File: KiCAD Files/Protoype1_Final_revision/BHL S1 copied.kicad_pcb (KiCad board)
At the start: 4 copper layers, 64 x 64 mm, 104 parts, among them IC1 NUP2105LT1G, IC2 NUP2105LT1G, IC4 FD6288Q, J1 39-30-1042, J2 Conn_01x03_Pin, J3 Conn_01x03_Pin, J4 39-30-1042, Q1 CSD19502Q5B, Q2 CSD19502Q5B, Q3 CSD19502Q5B, Q4 CSD19502Q5B, Q5 CSD19502Q5B, Q7 CSD19502Q5B, SW1 PTS636 SM50J SMTR LFS, U1 ME6211C30M5, U2 SPX3819M5-L-5-0, U3 Solder Pad, U5 STM32G431CBU6, Y1 8MHz

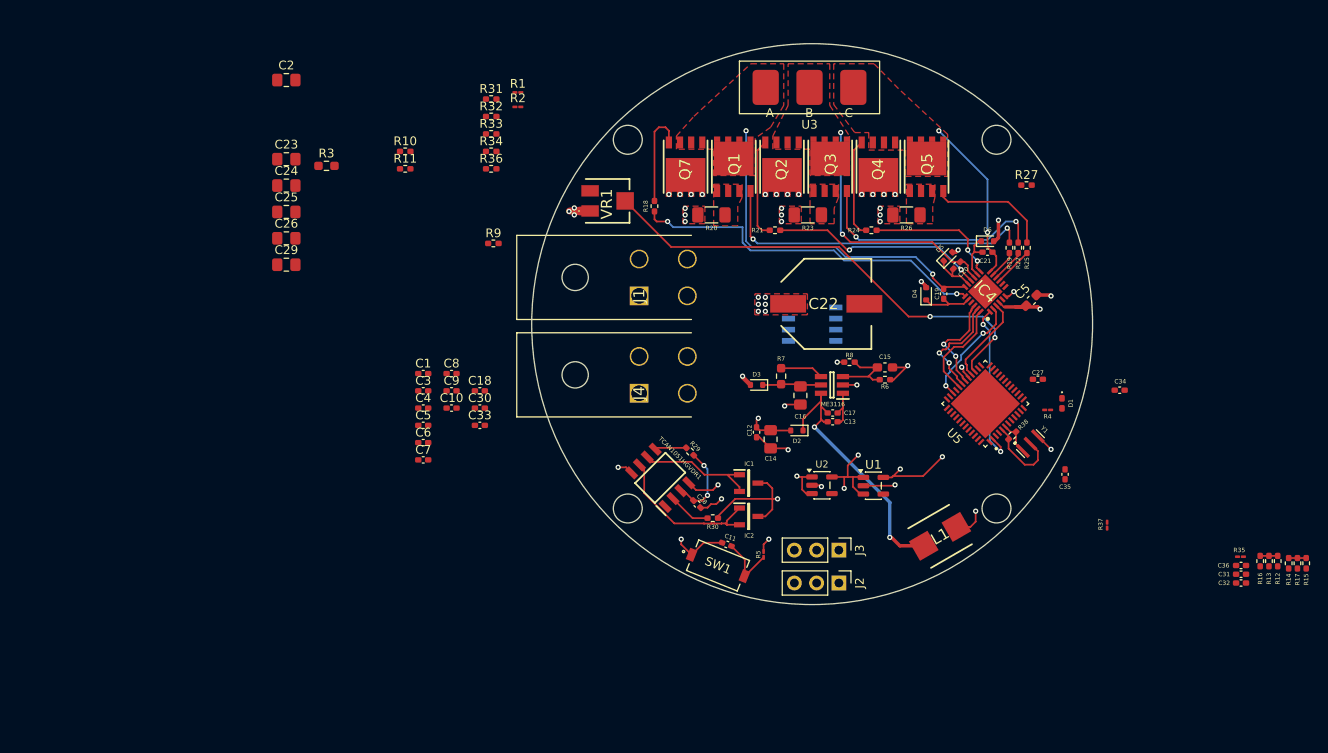
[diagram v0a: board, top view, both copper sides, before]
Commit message: Finished Routing the Magnetic Encoder and part of the STM32
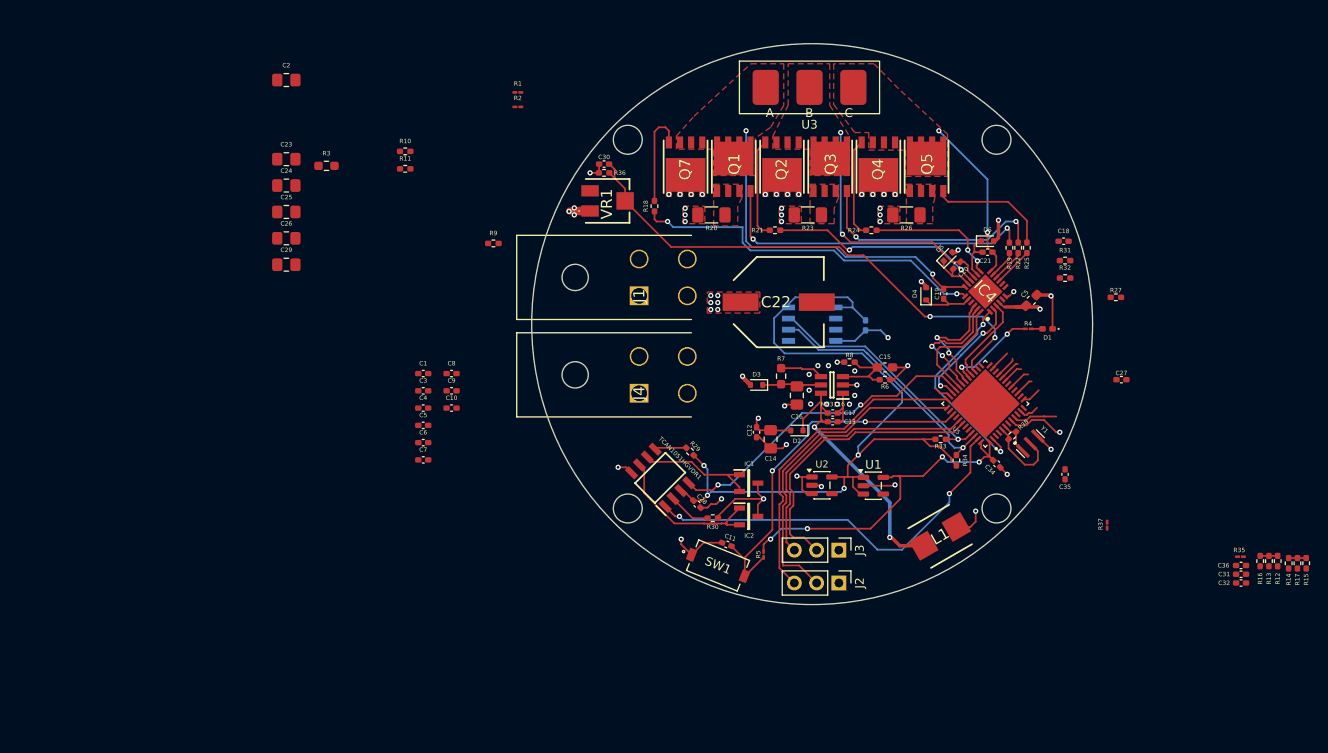
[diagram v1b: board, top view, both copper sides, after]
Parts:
- C33: moved to B.Cu
- moved C18 68.8 mm to (226.4, 74.0)
- moved R31 68.0 mm to (226.6, 76.2)
- moved R32 68.0 mm to (226.6, 78.2)
- moved R34 63.7 mm to (214.2, 99.0), turned to -90 degrees
- moved R33 62.0 mm to (212.4, 96.6), turned to 180 degrees
- moved C33 45.5 mm to (203.8, 83.6), turned to -90 degrees
- moved C30 31.2 mm to (174.0, 65.2), turned to 180 degrees
- moved R27 16.4 mm to (232.4, 80.4)
- moved C34 16.4 mm to (218.8, 99.4), turned to -45 degrees
- moved R36 12.9 mm to (174.0, 66.2)
- moved C27 9.53 mm to (233.0, 89.8)
- moved R4 9.51 mm to (222.4, 84.0)
- moved D1 8.66 mm to (224.6, 84.0), turned to 180 degrees
- moved C22 5.43 mm to (193.9, 81.0)
- moved C16 0.40 mm to (196.0, 91.6)
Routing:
- net VCC_5V: track 35.5 -> 94.1 mm
- net CAN_TX: track 0.00 -> 45.3 mm, vias 0 -> 2
- net SWCLK: track 0.00 -> 37.5 mm
- net SWDIO: track 0.00 -> 36.5 mm
- net BUTTON: track 7.15 -> 42.5 mm, vias 0 -> 2
- net Net-(J3-Pin_2): track 0.00 -> 33.2 mm
- net CAN_RX: track 3.93 -> 36.9 mm, vias 1 -> 2
- net USART2_TX: track 0.00 -> 31.8 mm
- net SDA: track 0.00 -> 29.1 mm, vias 0 -> 1
- net SCLK: track 0.00 -> 28.3 mm, vias 0 -> 1
- net GND: track 48.8 -> 65.9 mm, vias 22 -> 35
- net +3.3V: track 30.0 -> 43.6 mm, vias 3 -> 4
- net STATUS: track 1.59 -> 10.6 mm, vias 1 -> 2
- net VBUS: track 0.00 -> 6.60 mm, vias 0 -> 1
- net TEMP_FEEDBACK: track 54.4 -> 60.2 mm
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
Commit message: Finished the Board!!
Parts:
- removed C10, C6, C7, C8, C9: 0.1uF, Capacitor_SMD:C_0402_1005Metric_Pad0.74x0.62mm_HandSolder
- removed C29: 10uF/35V, Capacitor_SMD:C_0805_2012Metric_Pad1.18x1.45mm_HandSolder
- removed the C5 at (153.4, 95.0)
- removed R1: 0, Resistor_SMD:R_01005_0402Metric_Pad0.57x0.30mm_HandSolder
- removed R2: 10K, Resistor_SMD:R_01005_0402Metric_Pad0.57x0.30mm_HandSolder
- removed R27: 0, Resistor_SMD:R_0402_1005Metric_Pad0.72x0.64mm_HandSolder
- removed R3: 1M, Resistor_SMD:R_0603_1608Metric_Pad0.98x0.95mm_HandSolder
- C2: footprint Capacitor_SMD:C_0805_2012Metric_Pad1.18x1.45mm_HandSolder -> Capacitor_SMD:C_0402_1005Metric_Pad0.74x0.62mm_HandSolder
- moved C2 85.9 mm to (208.6, 104.2), turned to -90 degrees
- moved R10 80.8 mm to (226.6, 93.0), turned to 45 degrees
- moved R11 79.2 mm to (225.9, 92.3), turned to -135 degrees
- moved R9 67.7 mm to (228.6, 82.2), turned to 90 degrees
- moved C1 58.2 mm to (209.6, 104.2), turned to -90 degrees
- moved C23 56.4 mm to (188.2, 89.8)
- moved C24 55.9 mm to (188.2, 91.8)
- moved C25 55.5 mm to (188.2, 93.8)
- moved C26 55.1 mm to (188.2, 95.8)
- moved C3 51.1 mm to (202.8, 104.2), turned to -90 degrees
- moved C4 49.7 mm to (201.8, 104.2), turned to -90 degrees
- moved R15 39.7 mm to (226.6, 82.2), turned to 90 degrees
- moved R12 36.6 mm to (227.6, 82.2), turned to 90 degrees
- moved C36 36.0 mm to (220.6, 86.2), turned to 45 degrees
- moved R17 35.8 mm to (227.0, 86.2), turned to -90 degrees
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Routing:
- net +3.3V: track 43.6 -> 110.0 mm, vias 4 -> 7
- net Vshunt_1+: track 0.00 -> 51.8 mm, vias 0 -> 2
- net GND: track 65.9 -> 114.8 mm, vias 35 -> 54
- net Vshunt_2+: track 0.00 -> 39.5 mm, vias 0 -> 2
- net CAN_H: track 18.4 -> 57.4 mm
- net VBUS: track 6.60 -> 44.0 mm, vias 1 -> 2
- net VCC_12V: track 65.0 -> 100.5 mm
- net Vshunt_3+: track 0.00 -> 27.9 mm, vias 0 -> 2
- net CAN_L: track 14.0 -> 41.4 mm
- net DCBUS: track 5.17 -> 21.7 mm, vias 22 -> 26
- net Curr_fdbk1_OPAmp+: track 5.11 -> 21.0 mm, vias 0 -> 2
- net Net-(U5-PG10-~{RST}): track 0.00 -> 14.3 mm
- net Curr_fdbk3_OPAmp+: track 4.53 -> 18.5 mm, vias 0 -> 2
- net Curr_fdbk2_OPAmp+: track 4.19 -> 17.5 mm, vias 0 -> 2
- net Net-(U5-VDDA): track 4.92 -> 12.1 mm
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
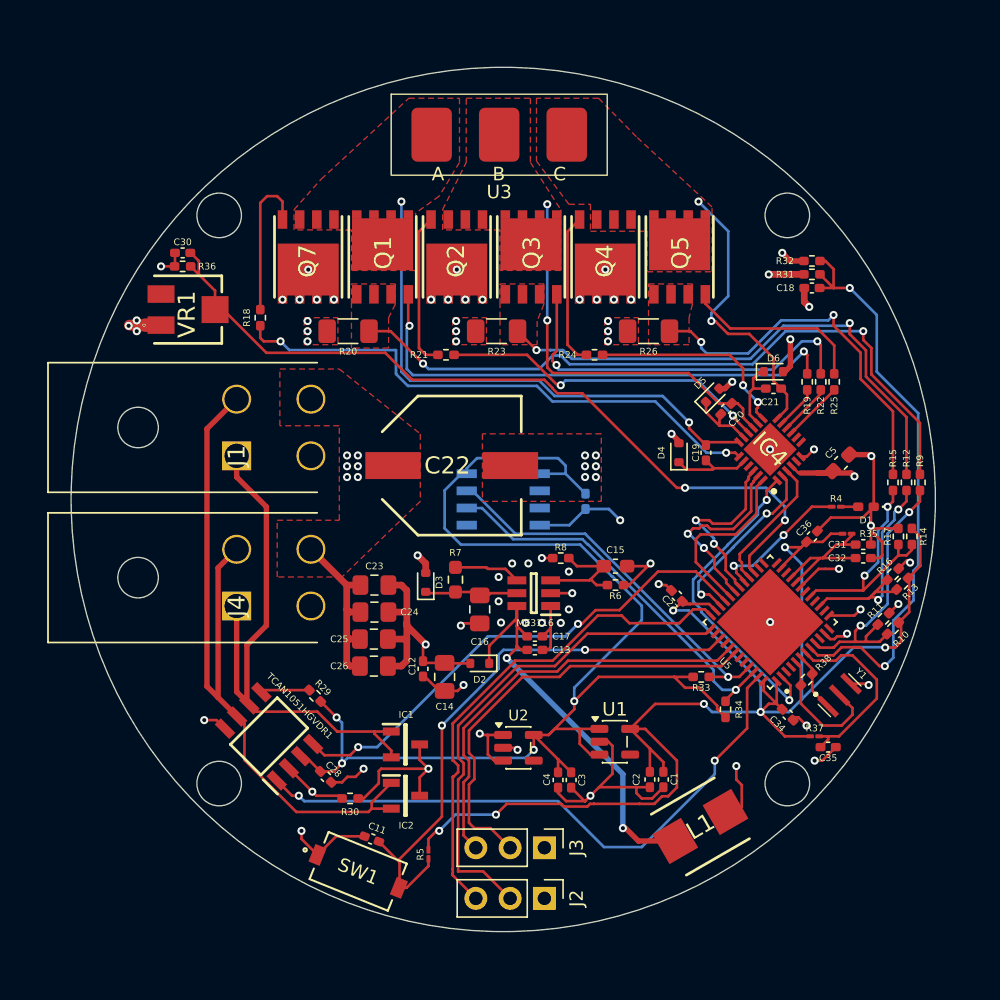
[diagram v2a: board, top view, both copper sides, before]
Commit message: Finished PCB. Enlargened diameter to 70mm.
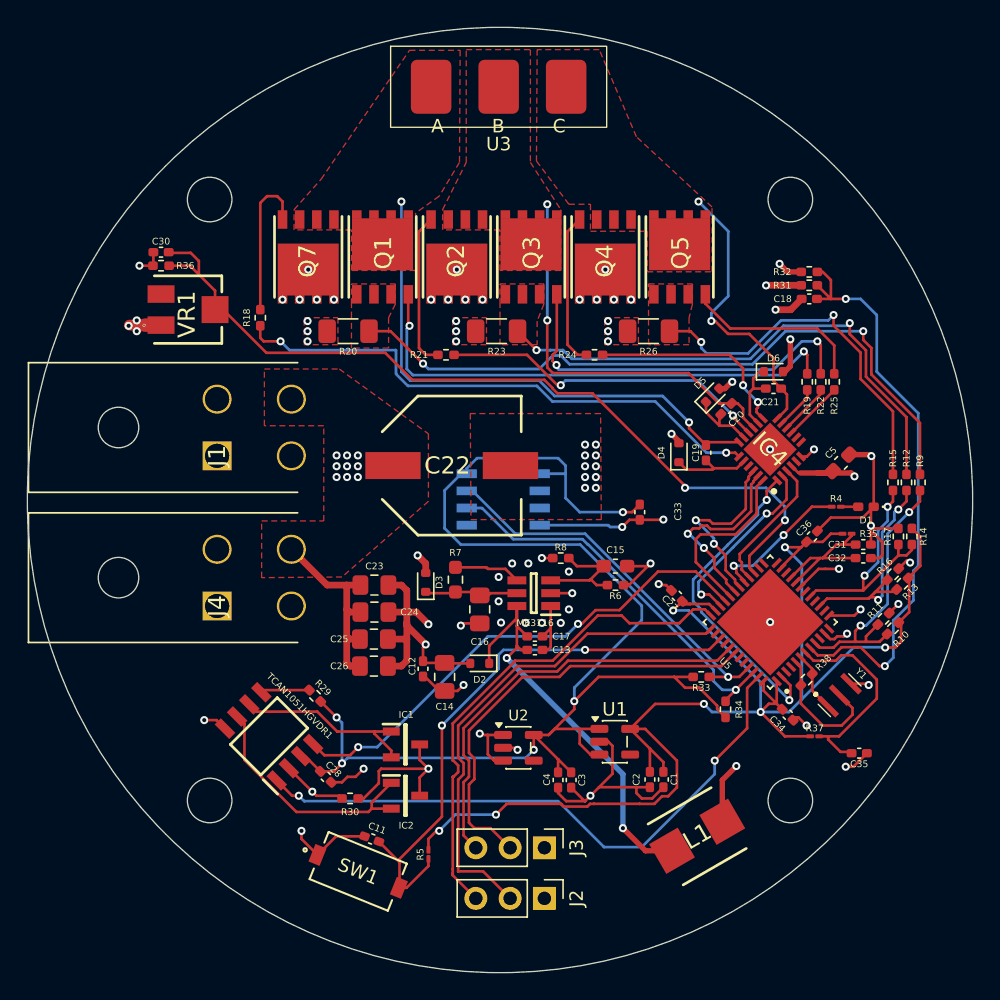
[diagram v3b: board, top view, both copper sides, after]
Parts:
- C33: moved to F.Cu
- moved C33 4.10 mm to (207.8, 84.4)
- moved U3 3.55 mm to (197.4, 52.9)
- moved C35 2.34 mm to (224.1, 102.2)
- moved C30 1.60 mm to (172.4, 65.2)
- moved R36 1.60 mm to (172.4, 66.2)
- moved J1 1.45 mm to (176.6, 80.2)
- moved J4 1.45 mm to (176.6, 91.3)
- moved C18 0.83 mm to (220.4, 68.6)
- moved R32 0.83 mm to (220.4, 66.6)
- moved R31 0.83 mm to (220.4, 67.6)
- moved L1 0.76 mm to (212.1, 108.4)
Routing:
- net CAN_H: track 57.4 -> 18.5 mm
- net CAN_L: track 41.4 -> 14.0 mm
- net VCC_5V: track 99.5 -> 105.3 mm, vias 4 -> 5
- net GND: track 114.8 -> 120.1 mm, vias 54 -> 60
- net TEMP_FEEDBACK: track 60.2 -> 63.5 mm
- net DCBUS: track 21.7 -> 23.1 mm, vias 26 -> 29
- net Net-(U5-PG10-~{RST}): track 14.3 -> 15.7 mm
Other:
- board size 64 x 64 mm -> 70 x 70 mm

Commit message: Final Revision of PCB
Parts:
- moved AS5600 56.4 mm to (142.6, 95.3)
- moved C13 56.4 mm to (145.0, 106.5)
- moved C14 56.4 mm to (138.3, 108.5)
- moved C17 56.4 mm to (145.0, 105.5)
- moved C31 56.4 mm to (169.3, 98.7)
- moved C32 56.4 mm to (169.3, 99.7)
- moved J4 56.4 mm to (121.4, 103.2)
- moved R11 56.4 mm to (170.8, 104.2)
- moved R30 56.4 mm to (131.3, 117.5)
- moved R31 56.4 mm to (165.3, 79.5)
- moved R33 56.4 mm to (157.3, 108.5)
- moved R6 56.4 mm to (150.9, 101.7)
- moved U2 56.4 mm to (143.7, 113.7)
- moved U3 56.4 mm to (142.3, 64.8)
- moved C12 56.4 mm to (136.7, 107.8)
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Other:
- outline, holes or cut-outs redrawn

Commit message: Finished Revision
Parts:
- R20, R23, R26: footprint Resistor_SMD:R_1206_3216Metric_Pad1.30x1.75mm_HandSolder -> Resistor_SMD:R_2512_6332Metric_Pad1.40x3.35mm_HandSolder
- moved R18 4.65 mm to (124.6, 77.2)
- moved R20 2.36 mm to (128.8, 83.5)
- moved R21 1.81 mm to (138.6, 86.4)
- moved J1 1.56 mm to (121.1, 93.6)
- moved J4 1.56 mm to (121.1, 104.7)
- moved R24 1.40 mm to (149.4, 86.0)
- moved R23 1.11 mm to (141.2, 83.5)
- moved R26 0.90 mm to (154.2, 83.2)
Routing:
- net CAN_H: track 18.5 -> 46.7 mm
- net CAN_L: track 14.0 -> 37.5 mm
- net DCBUS: track 23.1 -> 33.7 mm, vias 29 -> 60
- net GH_A: track 41.0 -> 47.9 mm
- net Net-(Q7-G): track 11.3 -> 6.60 mm
- net Net-(Q2-G): track 11.5 -> 14.9 mm
- net Vshunt_3+: track 27.9 -> 25.2 mm
- net TEMP_FEEDBACK: track 63.5 -> 65.9 mm, vias 2 -> 3
- net SH_C: track 21.2 -> 19.1 mm
- net SH_A: track 40.2 -> 41.9 mm
- net Net-(Q1-G): track 37.7 -> 39.4 mm
- net Net-(Q4-G): track 11.4 -> 12.7 mm
- net Vshunt_2+: track 39.5 -> 38.4 mm
- net GH_C: track 15.2 -> 14.2 mm
- net GH_B: track 24.5 -> 23.6 mm
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
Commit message: Position adjusted slightly
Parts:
- moved J1 2.13 mm to (122.1, 91.7)
- moved J4 1.88 mm to (122.0, 103.0)
- moved C30 1.57 mm to (115.8, 76.4)
- moved R36 1.57 mm to (115.8, 77.4)
- moved VR1 1.57 mm to (117.8, 80.6)
- moved R20 1.43 mm to (129.1, 82.1)
- moved Q2 1.26 mm to (139.2, 76.1)
- moved Q7 1.25 mm to (128.2, 76.1)
- moved Q3 1.25 mm to (144.7, 76.1)
- moved Q1 1.22 mm to (133.7, 76.1)
- moved Q4 1.18 mm to (150.2, 76.2)
- moved Q5 1.08 mm to (155.7, 76.3)
- moved R23 0.71 mm to (141.2, 82.8)
- moved R26 0.67 mm to (154.2, 82.5)
- moved R18 0.65 mm to (124.1, 77.6)
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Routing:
- net CAN_H: track 46.7 -> 51.4 mm
- net SH_B: track 29.4 -> 33.2 mm
- net Net-(Q2-G): track 14.9 -> 18.5 mm
- net SH_C: track 19.1 -> 21.4 mm
- net Net-(Q1-G): track 39.4 -> 41.3 mm
- net Net-(Q7-G): track 6.60 -> 4.94 mm
- net Net-(Q3-G): track 27.8 -> 29.0 mm
- net SH_A: track 41.9 -> 43.2 mm
- net TEMP_FEEDBACK: track 65.9 -> 67.1 mm
- net Net-(Q4-G): track 12.7 -> 13.9 mm
- net CAN_L: track 37.5 -> 36.4 mm
- net Vshunt_1+: track 52.4 -> 53.3 mm
- net Vshunt_3+: track 25.2 -> 25.9 mm
- net GH_A: track 47.9 -> 48.5 mm

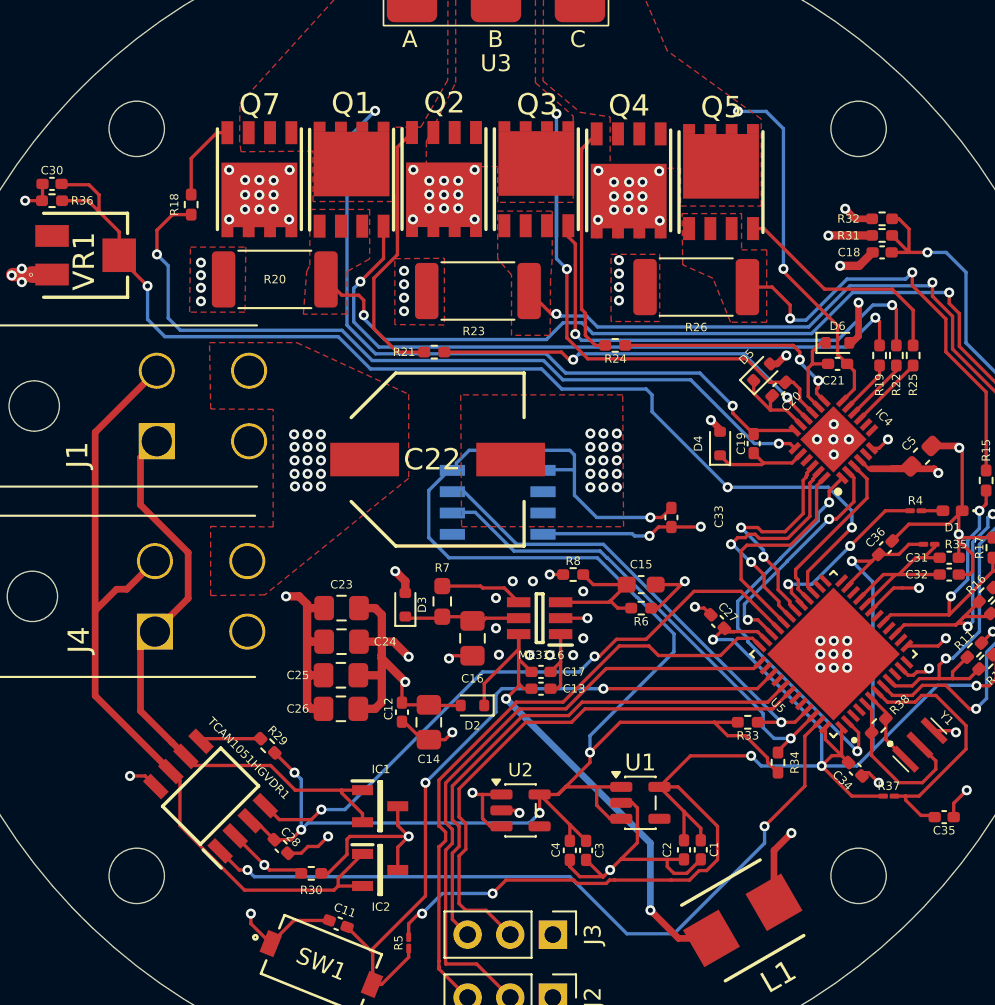
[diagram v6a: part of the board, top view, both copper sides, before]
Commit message: screw hole fixed
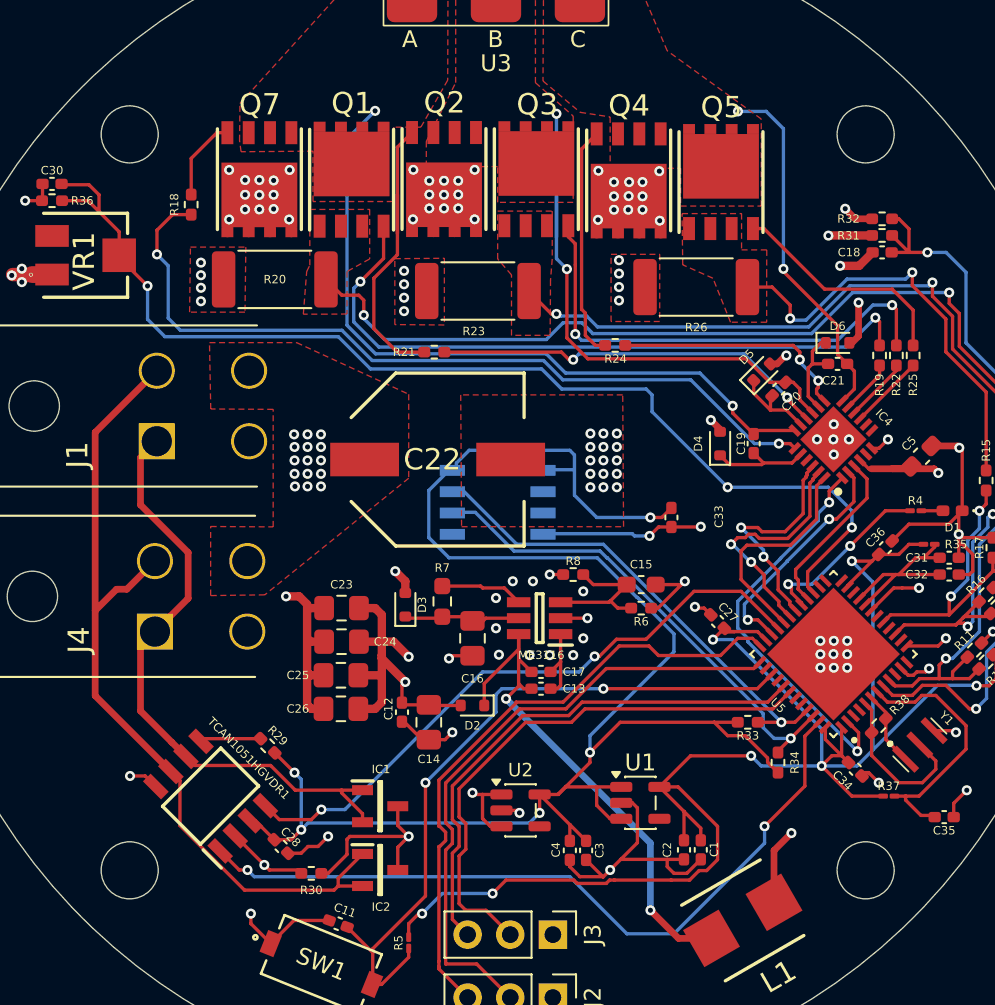
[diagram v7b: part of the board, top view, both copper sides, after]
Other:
- outline, holes or cut-outs redrawn
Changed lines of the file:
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@@
 	)
 	(gr_circle
-		(center 163.875603 73.1)
-		(end 166.875603 73.1)
-		(stroke
-			(width 0.05)
-			(type solid)
-		)
-		(fill no)
-		(layer "Dwgs.User")
-	)
-	(gr_circle
-		(center 120.875603 73.1)
-		(end 123.875603 73.1)
-		(stroke
-			(width 0.05)
-			(type solid)
-		)
-		(fill no)
-		(layer "Dwgs.User")
-	)
-	(gr_circle
-		(center 163.875603 117.6)
-		(end 166.875603 117.6)
-		(stroke
-			(width 0.05)
-			(type solid)
-		)
-		(fill no)
-		(layer "Dwgs.User")
-	)
-	(gr_circle
-		(center 120.875603 117.6)
-		(end 123.875603 117.6)
-		(stroke
-			(width 0.05)
-			(type solid)
-		)
-		(fill no)
-		(layer "Dwgs.User")
-	)
-	(gr_circle
-		(center 120.875603 117.6)
-		(end 122.525603 117.6)
+		(center 120.455293 117.27031)
+		(end 122.155293 117.27031)
 		(stroke
 			(width 0.05)
@@
 	)
 	(gr_circle
-		(center 163.875603 117.6)
-		(end 165.525603 117.6)
+		(center 120.455293 73.42969)
+		(end 122.155293 73.42969)
 		(stroke
 			(width 0.05)
@@
 	)
 	(gr_circle
-		(center 163.875603 73.1)
-		(end 165.525603 73.1)
+		(center 164.295913 117.27031)
+		(end 165.995913 117.27031)
 		(stroke
 			(width 0.05)
@@
 	)
 	(gr_circle
-		(center 120.875603 73.1)
-		(end 122.525603 73.1)
+		(center 164.295913 73.42969)
+		(end 165.995913 73.42969)
 		(stroke
 			(width 0.05)
@@
 		)
 	)
+	(group ""
+		(members "34532c9d-2bd0-40de-9b7f-24f7e803c8f7" "5a4a216e-e464-4c36-a9b1-1046fd16ec6d"
+			"5e78c962-8534-44f7-a47d-bf5676a943b7" "65e6da4c-c4bf-49a2-afb9-0f6ffc966b28"
+			"d595ccbd-10fc-4afa-b433-e8b2039c5b21"
+		)
+	)
